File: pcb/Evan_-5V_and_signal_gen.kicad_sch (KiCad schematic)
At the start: 33 parts, among them IC1 TL7660IDGKR, IC2 TL081IDT, IC4 UA78M33CDCYG3, IC9 TL081IDT, U5 TPS2069CDBVR_MOSFET

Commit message: Restructured PCB
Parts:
- added PWR1: Conn_01x03, Connector_PinHeader_2.54mm:PinHeader_1x03_P2.54mm_Vertical, symbol Connector_Generic:Conn_01x03
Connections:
- net +5V_EXT: now also PWR1.2 (Pin_2)
- net 3.3V Output: now also PWR1.3 (Pin_3)
- net GND: now also PWR1.1 (Pin_1)
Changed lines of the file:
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@@
 	(wire
 		(pts
+			(xy 132.08 180.34) (xy 135.89 180.34)
+		)
+		(stroke
+			(width 0)
+			(type default)
+		)
+	)
+	(wire
+		(pts
 			(xy 208.28 97.79) (xy 208.28 101.6)
 		)
@@
 	(wire
 		(pts
+			(xy 132.08 175.26) (xy 134.62 175.26)
+		)
+		(stroke
+			(width 0)
+			(type default)
+		)
+	)
+	(wire
+		(pts
 			(xy 30.734 29.972) (xy 26.924 29.972)
 		)
@@
 	(wire
 		(pts
+			(xy 132.08 177.8) (xy 134.62 177.8)
+		)
+		(stroke
+			(width 0)
+			(type default)
+		)
+	)
+	(wire
+		(pts
 			(xy 172.72 38.1) (xy 187.96 38.1)
 		)
@@
 		)
 	)
+	(global_label "+5V_EXT"
+		(shape input)
+		(at 134.62 177.8 0)
+		(fields_autoplaced yes)
+		(effects
+			(font
+				(size 1.27 1.27)
+			)
+			(justify left)
+		)
+		(property "Intersheetrefs" "${INTERSHEET_REFS}"
+			(at 145.7694 177.8 0)
+			(effects
+				(font
+					(size 1.27 1.27)
+				)
+				(justify left)
+				(hide yes)
+			)
+		)
+	)
+	(global_label "3.3V Output"
+		(shape input)
+		(at 134.62 175.26 0)
+		(fields_autoplaced yes)
+		(effects
+			(font
+				(size 1.27 1.27)
+			)
+			(justify left)
+		)
+		(property "Intersheetrefs" "${INTERSHEET_REFS}"
+			(at 148.9141 175.26 0)
+			(effects
+				(font
+					(size 1.27 1.27)
+				)
+				(justify left)
+				(hide yes)
+			)
+		)
+	)
 	(symbol
 		(lib_id "capstone:T495D106K035ATE300")
@@
 	)
 	(symbol
+		(lib_id "Connector_Generic:Conn_01x03")
+		(at 127 177.8 180)
+		(unit 1)
+		(exclude_from_sim no)
+		(in_bom yes)
+		(on_board yes)
+		(dnp no)
+		(property "Reference" "PWR1"
+			(at 121.666 177.8 0)
+			(effects
+				(font
+					(size 1.27 1.27)
+				)
+			)
+		)
+		(property "Value" "Conn_01x03"
+			(at 123.952 183.896 0)
+			(effects
+				(font
+					(size 1.27 1.27)
+				)
+			)
+		)
+		(property "Footprint" "Connector_PinHeader_2.54mm:PinHeader_1x03_P2.54mm_Vertical"
+			(at 127 177.8 0)
+			(effects
+				(font
+					(size 1.27 1.27)
+				)
+				(hide yes)
+			)
+		)
+		(property "Datasheet" "~"
+			(at 127 177.8 0)
+			(effects
+				(font
+					(size 1.27 1.27)
+				)
+				(hide yes)
+			)
+		)
+		(property "Description" ""
+			(at 127 177.8 0)
+			(effects
+				(font
+					(size 1.27 1.27)
+				)
+				(hide yes)
+			)
+		)
+		(pin "1"
+		)
+		(pin "2"
+		)
+		(pin "3"
+		)
+		(instances
+			(project "mcu_integration"
+				(path "/c0210bc3-f67f-47d8-a34e-f002a728adb2/39708197-8fe0-4b5c-ba49-65ed06982da9"
+					(reference "PWR1")
+					(unit 1)
+				)
+			)
+		)
+	)
+	(symbol
 		(lib_name "GND_1")
 		(lib_id "power:GND")
@@
 					(unit 1)
 				)
+			)
+		)
+	)
+	(symbol
+		(lib_name "GND_4")
+		(lib_id "power:GND")
+		(at 135.89 180.34 90)
+		(unit 1)
+		(exclude_from_sim no)
+		(in_bom yes)
+		(on_board yes)
+		(dnp no)
+		(fields_autoplaced yes)
+		(property "Reference" "#PWR066"
+			(at 142.24 180.34 0)
+			(effects
+				(font
+					(size 1.27 1.27)
+				)
+				(hide yes)
+			)
+		)
+		(property "Value" "GND"
+			(at 139.7 180.3399 90)
+			(effects
+				(font
+					(size 1.27 1.27)
+				)
+				(justify right)
+			)
+		)
+		(property "Footprint" ""
+			(at 135.89 180.34 0)
+			(effects
+				(font
+					(size 1.27 1.27)
+				)
+				(hide yes)
+			)
+		)
+		(property "Datasheet" ""
+			(at 135.89 180.34 0)
+			(effects
+				(font
+					(size 1.27 1.27)
+				)
+				(hide yes)
+			)
+		)
+		(property "Description" "Power symbol creates a global label with name \"GND\" , ground"
+			(at 135.89 180.34 0)
+			(effects
+				(font
+					(size 1.27 1.27)
+				)
+				(hide yes)
+			)
+		)
+		(pin "1"
+		)
+		(instances
+			(project ""
+				(path "/c0210bc3-f67f-47d8-a34e-f002a728adb2/39708197-8fe0-4b5c-ba49-65ed06982da9"
+					(reference "#PWR066")
+					(unit 1)
+				)

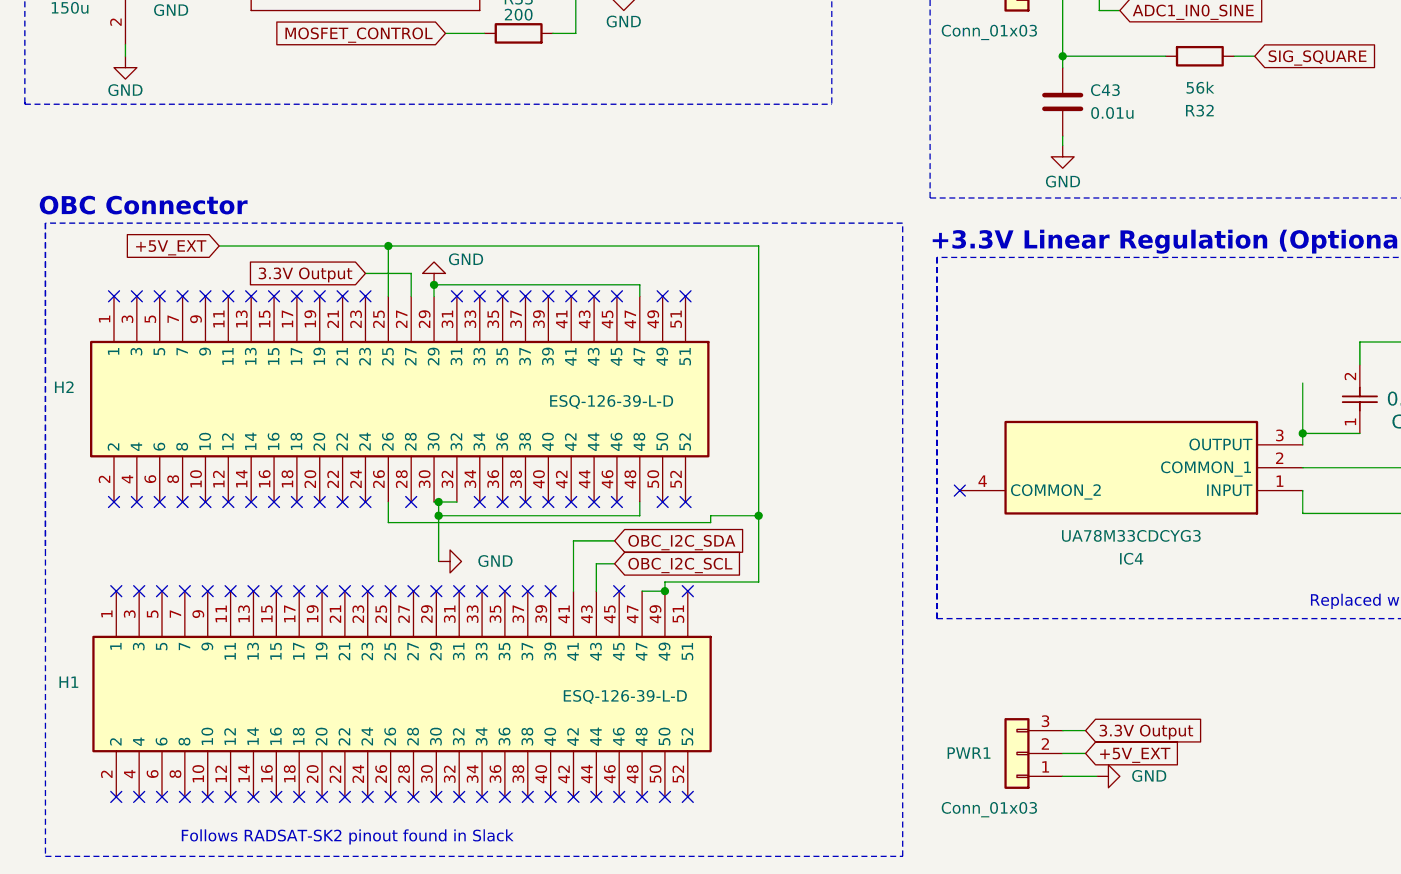
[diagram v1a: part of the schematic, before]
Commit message: Added I2C Connector
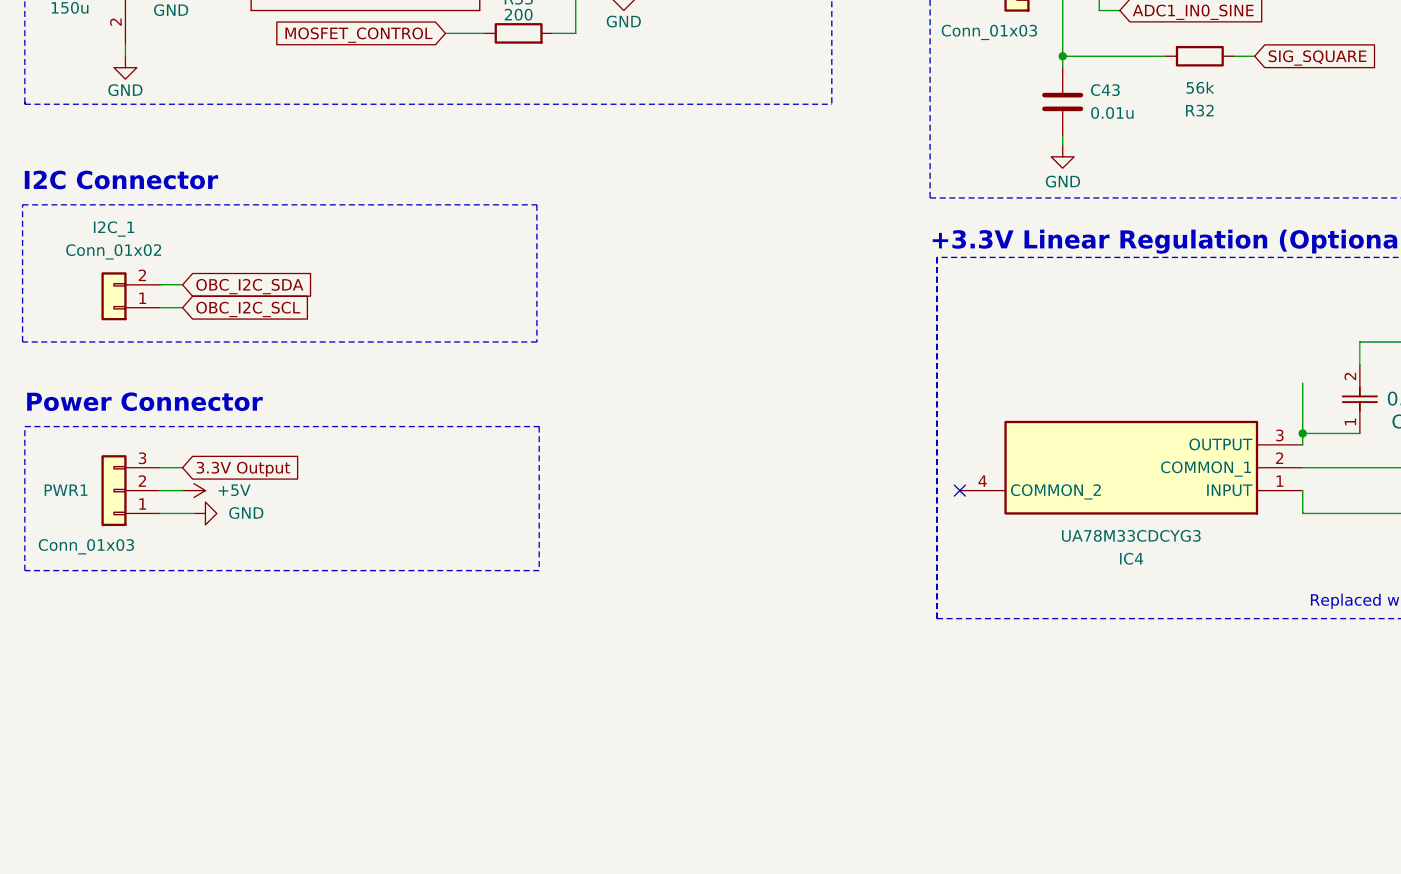
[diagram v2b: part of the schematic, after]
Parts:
- removed H1, H2: ESQ-126-39-L-D, capstone:ESQ-126-Y-X-D, symbol capstone:ESQ-126-39-L-D
- added I2C_1: Conn_01x02, Connector_PinHeader_2.54mm:PinHeader_1x02_P2.54mm_Vertical, symbol Connector_Generic:Conn_01x02
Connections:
- net +5V: now also PWR1.2 (Pin_2)
- net +5V_EXT: no longer PWR1.2 (Pin_2)
- net OBC_I2C_SCL: now also I2C_1.1 (Pin_1)
- net OBC_I2C_SDA: now also I2C_1.2 (Pin_2)
- no-connect marks 99 -> 7
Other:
- note added: "I2C Connector"
- note added: "Power Connector"
- note removed: "Follows RADSAT-SK2 pinout found in Slack"
- note removed: "OBC Connector"
- moved on the sheet: PWR1

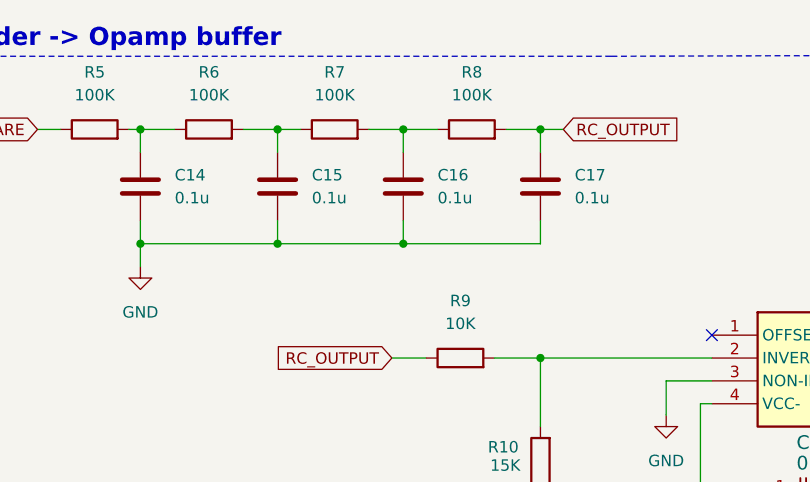
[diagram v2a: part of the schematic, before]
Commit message: Added reset button & LED, fixed SD card overhang
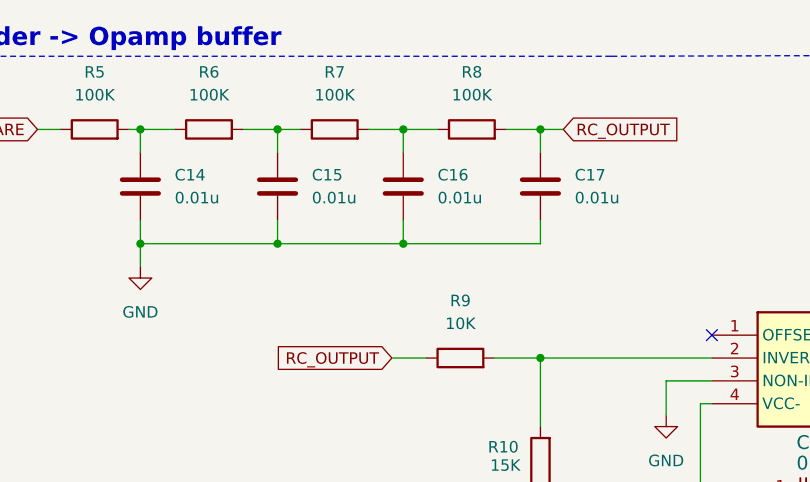
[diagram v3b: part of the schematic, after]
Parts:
- C14, C15, C16, C17: value 0.1u -> 0.01u
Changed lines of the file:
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@@
 			)
 		)
-		(property "Value" "0.1u"
+		(property "Value" "0.01u"
 			(at 162.56 33.0199 0)
 			(effects
@@
 			)
 		)
-		(property "Value" "0.1u"
+		(property "Value" "0.01u"
 			(at 191.77 33.0199 0)
 			(effects
@@
 			)
 		)
-		(property "Value" "0.1u"
+		(property "Value" "0.01u"
 			(at 176.53 33.0199 0)
 			(effects
@@
 			)
 		)
-		(property "Value" "0.1u"
+		(property "Value" "0.01u"
 			(at 147.32 33.0199 0)
 			(effects

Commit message: Added non-inverting amplifier
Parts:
- removed C45, C46: 0.1u, capstone:CAPC220145_88N_KEM-0.1u, symbol capstone:C0805C104K5RAC7210
- removed IC9: TL081IDT, capstone:SOIC127P600X175-8N, symbol capstone:TL081IDT
- removed R11, R12: 10K, Resistor_SMD:R_0402_1005Metric, symbol Device:R
- C14, C15, C16, C17: value 0.01u -> 0.47u
- R10: value 15K -> 9K
- R5, R6, R7, R8: value 100K -> 3.3K
- R9: value 10K -> 1K
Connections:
- net INVERT_SINE is gone; now on net ADC1_IN0_SINE: IC2.6 (OUTPUT), R10.1
- net +5V: now also C44.1
- net -5V Output: no longer C44.1
- net GND: now also R9.2; no longer IC2.3 (NON-INVERTING_INPUT)
- net RC_OUTPUT: now also IC2.3 (NON-INVERTING_INPUT); no longer R9.1
- net at IC2.2 (INVERTING_INPUT), R10.2: now also R9.1; no longer R9.2
- no-connect marks 7 -> 5

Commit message: changed footprints and layout
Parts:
- C12, C13: footprint capstone:T495D -> Capacitor_SMD:C_0805_2012Metric
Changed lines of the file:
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@@
 			)
 		)
-		(property "Footprint" "capstone:T495D"
+		(property "Footprint" "Capacitor_SMD:C_0805_2012Metric"
 			(at 173.66 45.72 0)
 			(effects
@@
 			)
 		)
-		(property "Footprint" "capstone:T495D"
+		(property "Footprint" "Capacitor_SMD:C_0805_2012Metric"
 			(at -69.266 38.862 0)
 			(effects

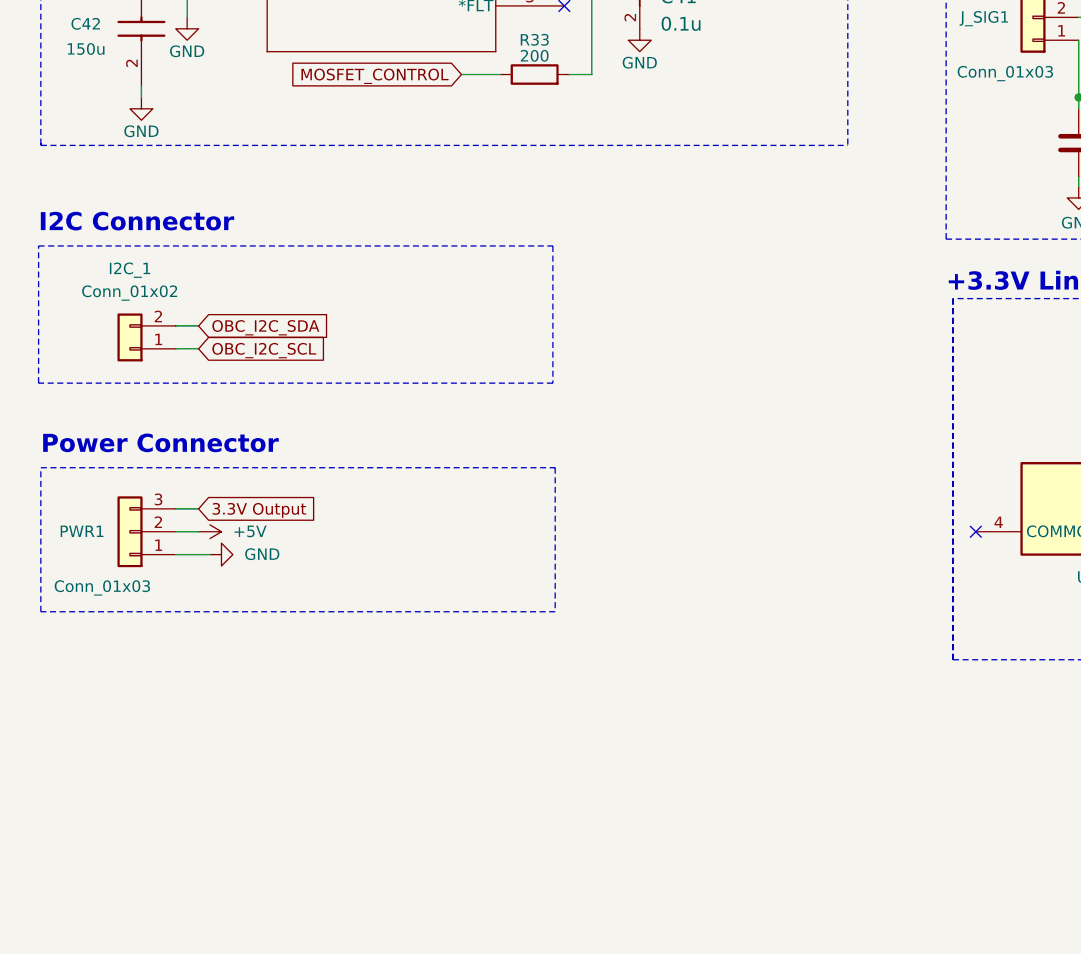
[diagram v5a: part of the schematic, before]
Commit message: Added Shields
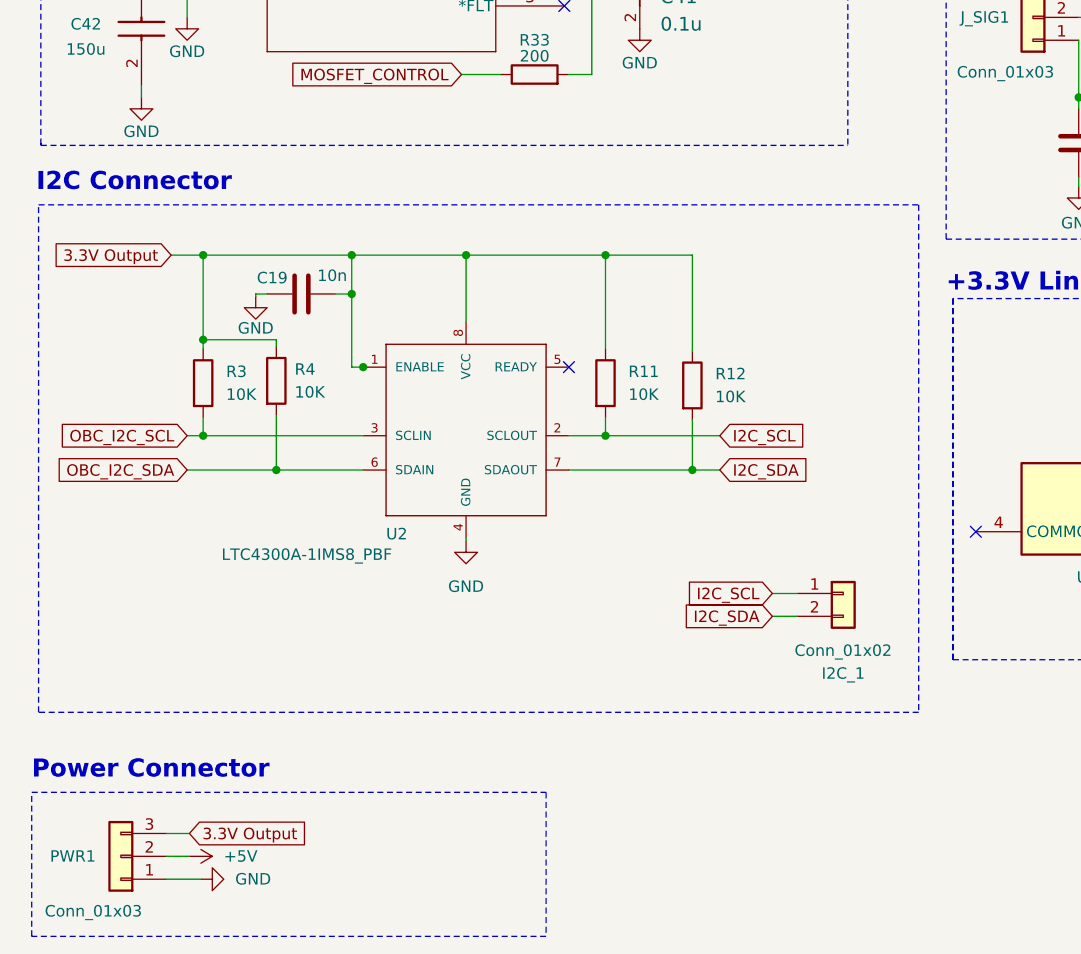
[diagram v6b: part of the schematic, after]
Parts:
- added C19: 10n, Capacitor_SMD:C_0402_1005Metric, symbol Device:C
- added R11, R12, R3, R4: 10K, Resistor_SMD:R_0402_1005Metric, symbol Device:R
- added U2: LTC4300A-1IMS8_PBF, capstone:LTC4300A-1IMS8_PBF, symbol capstone:LTC4300A-1IMS8_PBF
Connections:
- net 3.3V Output: now also C19.2, R11.1, R12.1, R3.1, R4.1, U2.1 (ENABLE), U2.8 (VCC)
- net GND: now also C19.1, U2.4 (GND)
- net OBC_I2C_SCL: now also R3.2, U2.3 (SCLIN); no longer I2C_1.1 (Pin_1)
- net OBC_I2C_SDA: now also R4.2, U2.6 (SDAIN); no longer I2C_1.2 (Pin_2)
- new net I2C_SCL: I2C_1.1 (Pin_1), R11.2, U2.2 (SCLOUT)
- new net I2C_SDA: I2C_1.2 (Pin_2), R12.2, U2.7 (SDAOUT)
- no-connect marks 5 -> 6
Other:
- moved on the sheet: I2C_1, PWR1
